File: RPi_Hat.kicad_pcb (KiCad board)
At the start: 2 copper layers, 74.1 x 56.5 mm, 32 parts, among them J3 RPi_GPIO, P1 3Sip100, P2 4Sip200, P3 2Sip200, P4 SMA, P5 CONN_01X02, Q1 BC807, U1 LM7805

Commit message: Placing components
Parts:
- moved R9 29.9 mm to (61.0, 76.2), turned to 0 degrees
- moved D1 26.0 mm to (59.7, 80.0), turned to 0 degrees
- moved C3 23.9 mm to (72.4, 62.2)
- moved L3 20.1 mm to (53.3, 74.9), turned to 270 degrees
- moved L4 18.2 mm to (47.0, 80.0)
- moved C6 17.7 mm to (54.6, 80.0), turned to 0 degrees
- moved L1 17.7 mm to (53.3, 58.4)
- moved C4 17.3 mm to (54.6, 62.2), turned to 0 degrees
- moved L2 17.2 mm to (53.3, 66.0)
- moved C2 16.6 mm to (69.8, 72.4), turned to 180 degrees
- moved R6 12.5 mm to (45.7, 76.2)
- moved C5 12.0 mm to (54.6, 69.8), turned to 0 degrees
- moved R7 8.64 mm to (44.5, 66.0), turned to 180 degrees
- moved R1 7.62 mm to (83.8, 45.7)
- moved R4 7.62 mm to (83.8, 38.1)
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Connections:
- U1 pad 1: (no net) -> Net-(C3-Pad1)
- U1 pad 2: (no net) -> GND
- U1 pad 3: (no net) -> +5V
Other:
- board size 74.1 x 56.5 mm -> 66 x 56.5 mm
- board text added: "http://www.giga.co.za ZR6AIC Raspberry Pi 2m TX"
- board text removed: "Dimensions taken from https://github.com/raspberrypi/hats/blob/master/hat-board-mechanical.pdf"
- board text removed: "Select one of these board edges depending upon the type of socket that is used."

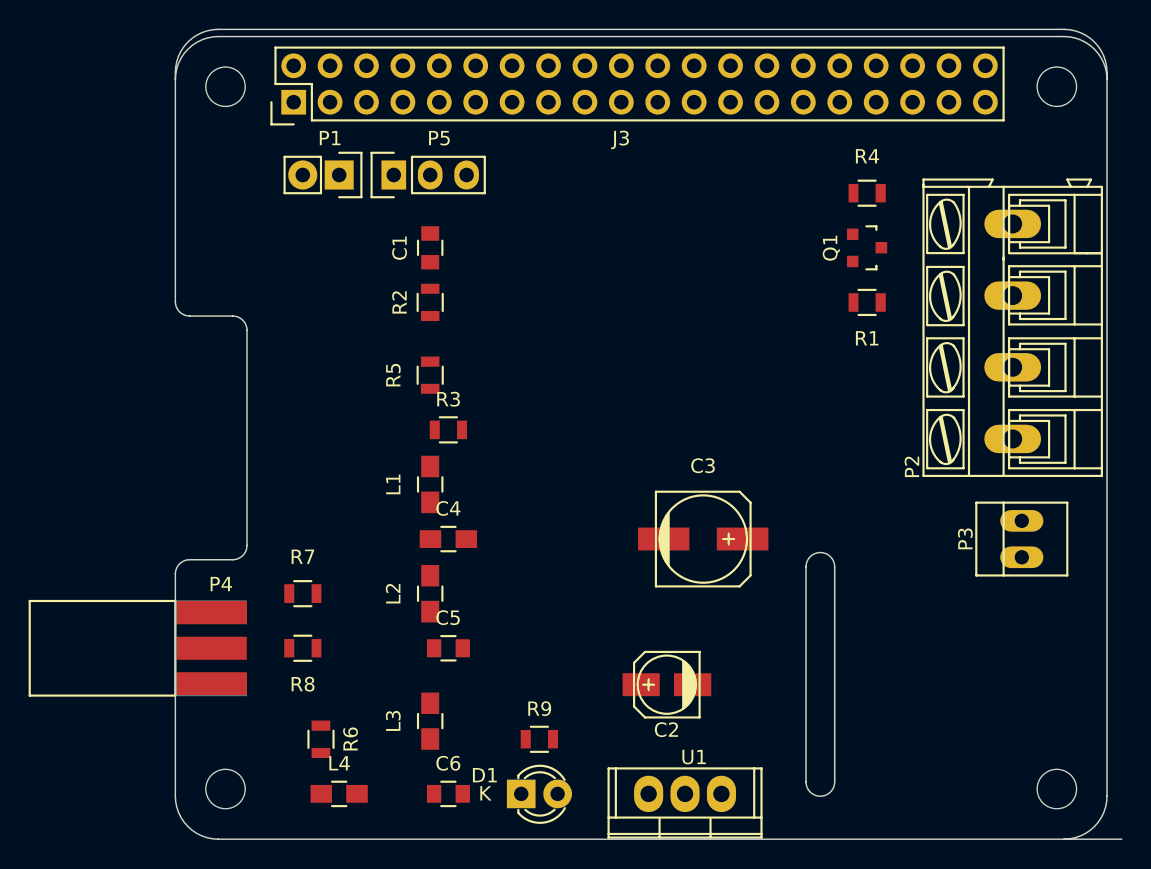
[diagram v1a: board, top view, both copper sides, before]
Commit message: Change Regulator transistor and connectors
Change Regulator transistor and connectors
Started laying out PCB
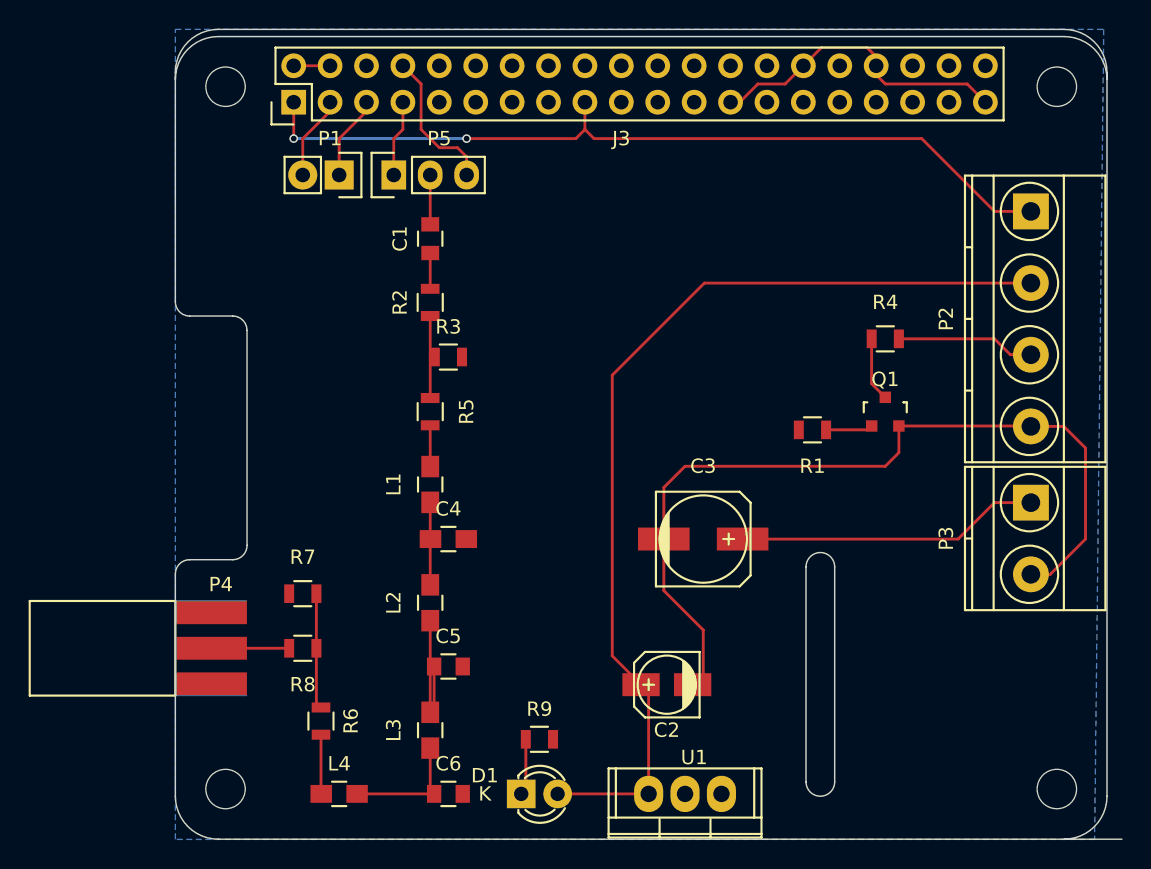
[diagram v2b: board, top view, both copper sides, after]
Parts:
- P2: footprint Connect:AK300-4 -> Terminal_Blocks:TerminalBlock_Pheonix_MKDS1.5-4pol
- P3: footprint Connect:PINHEAD1-2 -> Terminal_Blocks:TerminalBlock_Pheonix_MKDS1.5-2pol
- Q1: value BC807 -> BC817-40
- U1: value LM7805 -> L4940V5 1.5A
- moved P2 15.9 mm to (95.2, 39.4), turned to 270 degrees
- moved Q1 11.5 mm to (85.1, 53.3), turned to 0 degrees
- moved R4 10.2 mm to (85.1, 48.3)
- moved R1 9.67 mm to (80.0, 54.6)
- moved R3 5.08 mm to (54.6, 49.5)
- moved P3 2.62 mm to (95.2, 59.7), turned to 270 degrees
- moved R5 2.54 mm to (53.3, 53.3), turned to 90 degrees
- moved C5 1.27 mm to (54.6, 71.1)
- moved R6 1.27 mm to (45.7, 74.9)
- moved C1 0.63 mm to (53.3, 41.3)
- moved L2 0.63 mm to (53.3, 66.7)
- moved L3 0.63 mm to (53.3, 75.6)
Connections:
- Q1 pad 2: Net-(Q1-Pad2) -> GND
- Q1 pad 3: GND -> Net-(Q1-Pad3)
- R1 pad 1: Net-(Q1-Pad2) -> Net-(Q1-Pad1)
- R4 pad 2: Net-(Q1-Pad1) -> Net-(Q1-Pad3)
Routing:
- net GND: track 0.00 -> 84.2 mm
- net +5V: track 0.00 -> 71.0 mm
- net +3V3: track 0.00 -> 58.5 mm, vias 0 -> 2
- net Net-(C3-Pad1): track 0.00 -> 21.2 mm
- net Net-(J3-Pad8): track 0.00 -> 10.2 mm
- net Net-(C5-Pad1): track 0.00 -> 9.70 mm
- net Net-(P2-Pad3): track 0.00 -> 9.67 mm
- net Net-(C6-Pad1): track 0.00 -> 8.68 mm
- net Net-(R6-Pad1): track 0.00 -> 8.07 mm
- net Net-(J3-Pad5): track 0.00 -> 5.87 mm
- net Net-(J3-Pad3): track 0.00 -> 5.87 mm
- net Net-(C4-Pad1): track 0.00 -> 5.75 mm
- net Net-(R2-Pad1): track 0.00 -> 5.72 mm
- net Net-(P4-Pad1): track 0.00 -> 5.40 mm
- net Net-(J3-Pad7): track 0.00 -> 5.34 mm
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- added copper zone on B.Cu, net GND
